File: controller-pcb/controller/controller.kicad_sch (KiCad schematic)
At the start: 1 part

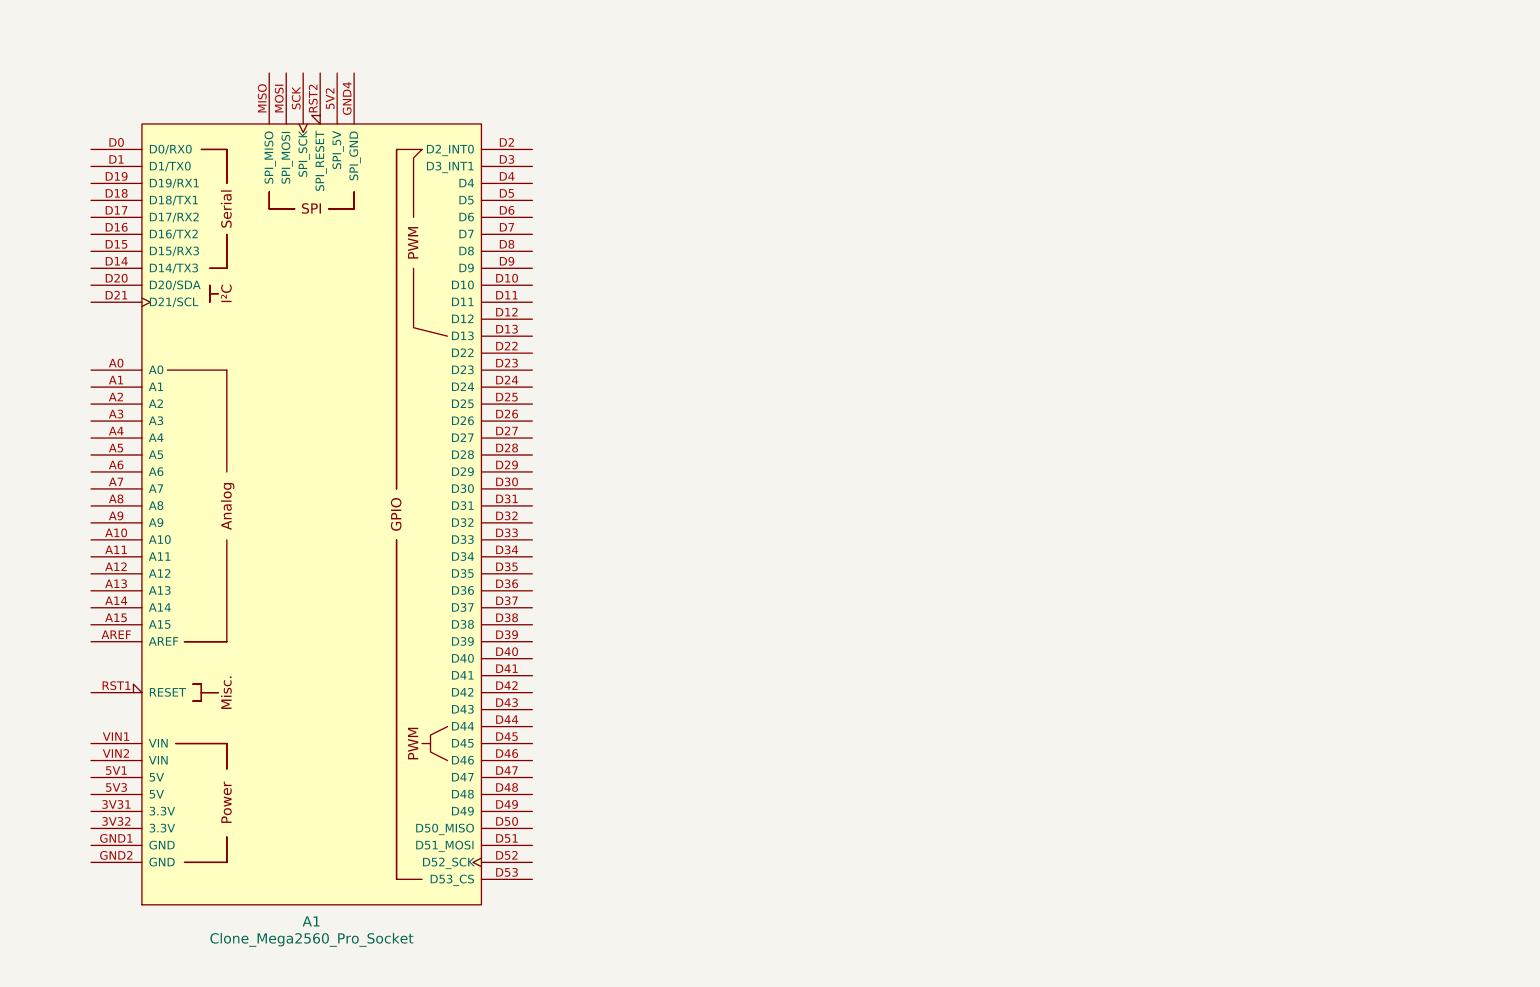
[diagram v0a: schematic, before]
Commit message: adding controller board pcb
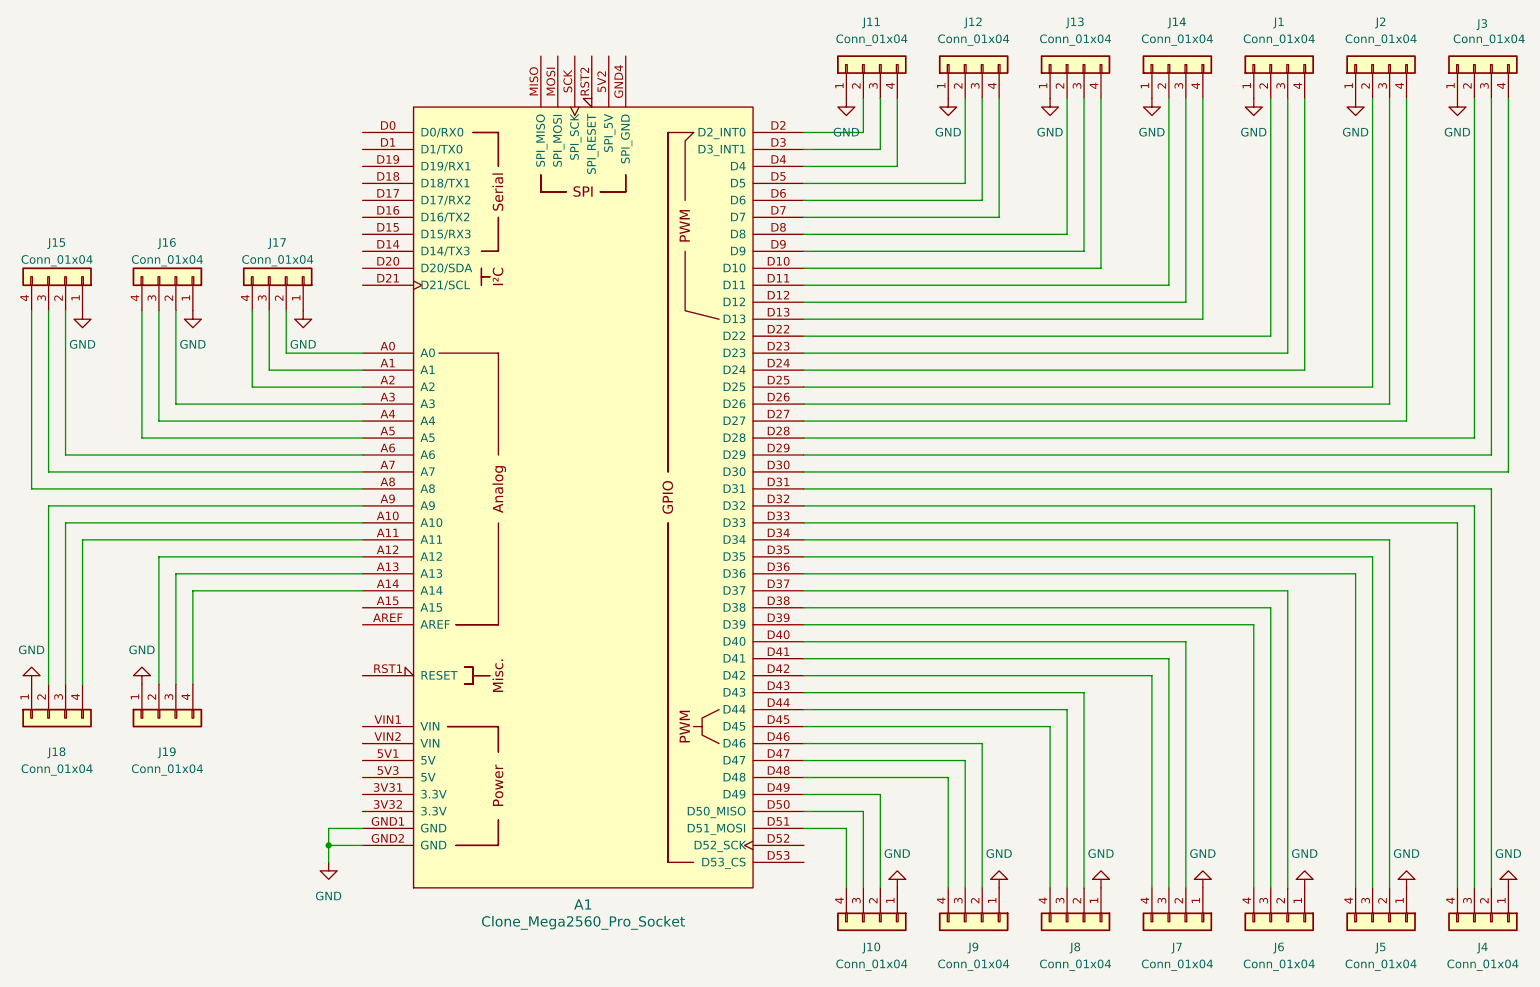
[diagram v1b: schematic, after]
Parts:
- added J1, J10, J11, J12, J13, J14, J15, J16, J17, J18, J19, J2, J3, J4, J5, J6, J7, J8, J9: Conn_01x04, Connector_JST:JST_ZH_B4B-ZR_1x04_P1.50mm_Vertical, symbol Connector_Generic:Conn_01x04
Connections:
- net at A1.A0: now also J17.2 (Pin_2)
- net at A1.A1: now also J17.3 (Pin_3)
- net at A1.A10: now also J18.3 (Pin_3)
- net at A1.A11: now also J18.4 (Pin_4)
- net at A1.A12: now also J19.2 (Pin_2)
- net at A1.A13: now also J19.3 (Pin_3)
- net at A1.A14: now also J19.4 (Pin_4)
- net at A1.A2: now also J17.4 (Pin_4)
- net at A1.A3: now also J16.2 (Pin_2)
- net at A1.A4: now also J16.3 (Pin_3)
- net at A1.A5: now also J16.4 (Pin_4)
- net at A1.A6: now also J15.2 (Pin_2)
- net at A1.A7: now also J15.3 (Pin_3)
- net at A1.A8: now also J15.4 (Pin_4)
- net at A1.A9: now also J18.2 (Pin_2)
- net at A1.D10: now also J13.4 (Pin_4)
- net at A1.D11: now also J14.2 (Pin_2)
- net at A1.D12: now also J14.3 (Pin_3)
- net at A1.D13: now also J14.4 (Pin_4)
- net at A1.D2 (D2_INT0): now also J11.2 (Pin_2)
- net at A1.D22: now also J1.2 (Pin_2)
- net at A1.D23: now also J1.3 (Pin_3)
- net at A1.D24: now also J1.4 (Pin_4)
- net at A1.D25: now also J2.2 (Pin_2)
- net at A1.D26: now also J2.3 (Pin_3)
- net at A1.D27: now also J2.4 (Pin_4)
- net at A1.D28: now also J3.2 (Pin_2)
- net at A1.D29: now also J3.3 (Pin_3)
- net at A1.D3 (D3_INT1): now also J11.3 (Pin_3)
- net at A1.D30: now also J3.4 (Pin_4)
- net at A1.D31: now also J4.2 (Pin_2)
- net at A1.D32: now also J4.3 (Pin_3)
- net at A1.D33: now also J4.4 (Pin_4)
- net at A1.D34: now also J5.2 (Pin_2)
- net at A1.D35: now also J5.3 (Pin_3)
- net at A1.D36: now also J5.4 (Pin_4)
- net at A1.D37: now also J6.2 (Pin_2)
- net at A1.D38: now also J6.3 (Pin_3)
- net at A1.D39: now also J6.4 (Pin_4)
- net at A1.D4: now also J11.4 (Pin_4)
- net at A1.D40: now also J7.2 (Pin_2)
- net at A1.D41: now also J7.3 (Pin_3)
- net at A1.D42: now also J7.4 (Pin_4)
- net at A1.D43: now also J8.2 (Pin_2)
- net at A1.D44: now also J8.3 (Pin_3)
- net at A1.D45: now also J8.4 (Pin_4)
- net at A1.D46: now also J9.2 (Pin_2)
- net at A1.D47: now also J9.3 (Pin_3)
- net at A1.D48: now also J9.4 (Pin_4)
- net at A1.D49: now also J10.2 (Pin_2)
- net at A1.D5: now also J12.2 (Pin_2)
- net at A1.D50 (D50_MISO): now also J10.3 (Pin_3)
- net at A1.D51 (D51_MOSI): now also J10.4 (Pin_4)
- net at A1.D6: now also J12.3 (Pin_3)
- net at A1.D7: now also J12.4 (Pin_4)
- net at A1.D8: now also J13.2 (Pin_2)
- net at A1.D9: now also J13.3 (Pin_3)
- net GND: now reaches A1.GND1 (GND)
- net GND: now also A1.GND2 (GND), J1.1 (Pin_1), J10.1 (Pin_1), J11.1 (Pin_1), J12.1 (Pin_1), J13.1 (Pin_1), J14.1 (Pin_1), J15.1 (Pin_1), J16.1 (Pin_1), J17.1 (Pin_1), J18.1 (Pin_1), J19.1 (Pin_1), J2.1 (Pin_1), J3.1 (Pin_1), J4.1 (Pin_1), J5.1 (Pin_1), J6.1 (Pin_1), J7.1 (Pin_1), J8.1 (Pin_1), J9.1 (Pin_1)
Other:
- moved on the sheet: A1
